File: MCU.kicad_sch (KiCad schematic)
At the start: 42 parts, among them J301 USB_C_Receptacle_USB2.0, J302 Conn_ARM_SWD_TagConnect_TC2030, J303 Screw_Terminal_01x06, SW301 SW_SPDT, U2 STM32H733VGTx, U301 USBLC6-2SC6, Y301 24MHz

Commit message: Refactoring
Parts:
- C301, C318, C319: JLCPCB Part # (none) -> C71001
- C302, C303, C304, C305, C306, C307, C308, C309, C310, C311, C312, C313, C316, C317: JLCPCB Part # (none) -> C432917
- C314, C315: value 14p -> 10p; JLCPCB Part # (none) -> C258501
- D302: JLCPCB Part # (none) -> C3021133; JLCPCB Part# C3021133 -> (none)
- D303: JLCPCB Part # (none) -> C5547384; JLCPCB Part# C5547384 -> (none)
- FB301, FB302: JLCPCB Part # (none) -> C12391
- FL301: JLCPCB Part # (none) -> C3211819; JLCPCB Part# C3211819 -> (none)
- J301: JLCPCB Part # (none) -> C165948; JLCPCB Part# C165948 -> (none)
- J303: JLCPCB Part # (none) -> C3817456; JLCPCB Part# C3817456 -> (none)
- R301: JLCPCB Part # (none) -> C176114
- R302, R305, R306, R307, R308: JLCPCB Part # (none) -> C103557
- R303, R304: JLCPCB Part # (none) -> C325521
- R309, R310: value 325R -> 325R (300R); JLCPCB Part # (none) -> C137637
- R311: JLCPCB Part # (none) -> C328375
- SW301: JLCPCB Part # (none) -> C221841; JLCPCB Part# C221841 -> (none)
- U2: JLCPCB Part # (none) -> C730160; JLCPCB Part# C730160 -> (none)
- U301: JLCPCB Part # (none) -> C5261088; JLCPCB Part# C5261088 -> (none)
- Y301: JLCPCB Part # (none) -> C5308005; JLCPCB Part# C5181479 -> (none)
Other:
- note added: "Cload = 2*(Co-Cs) Co = 10p Cs estimated to be 5p"
- note removed: "Cload = 2*(Co-Cs) Co = 12p Cs estimated to be 5p"

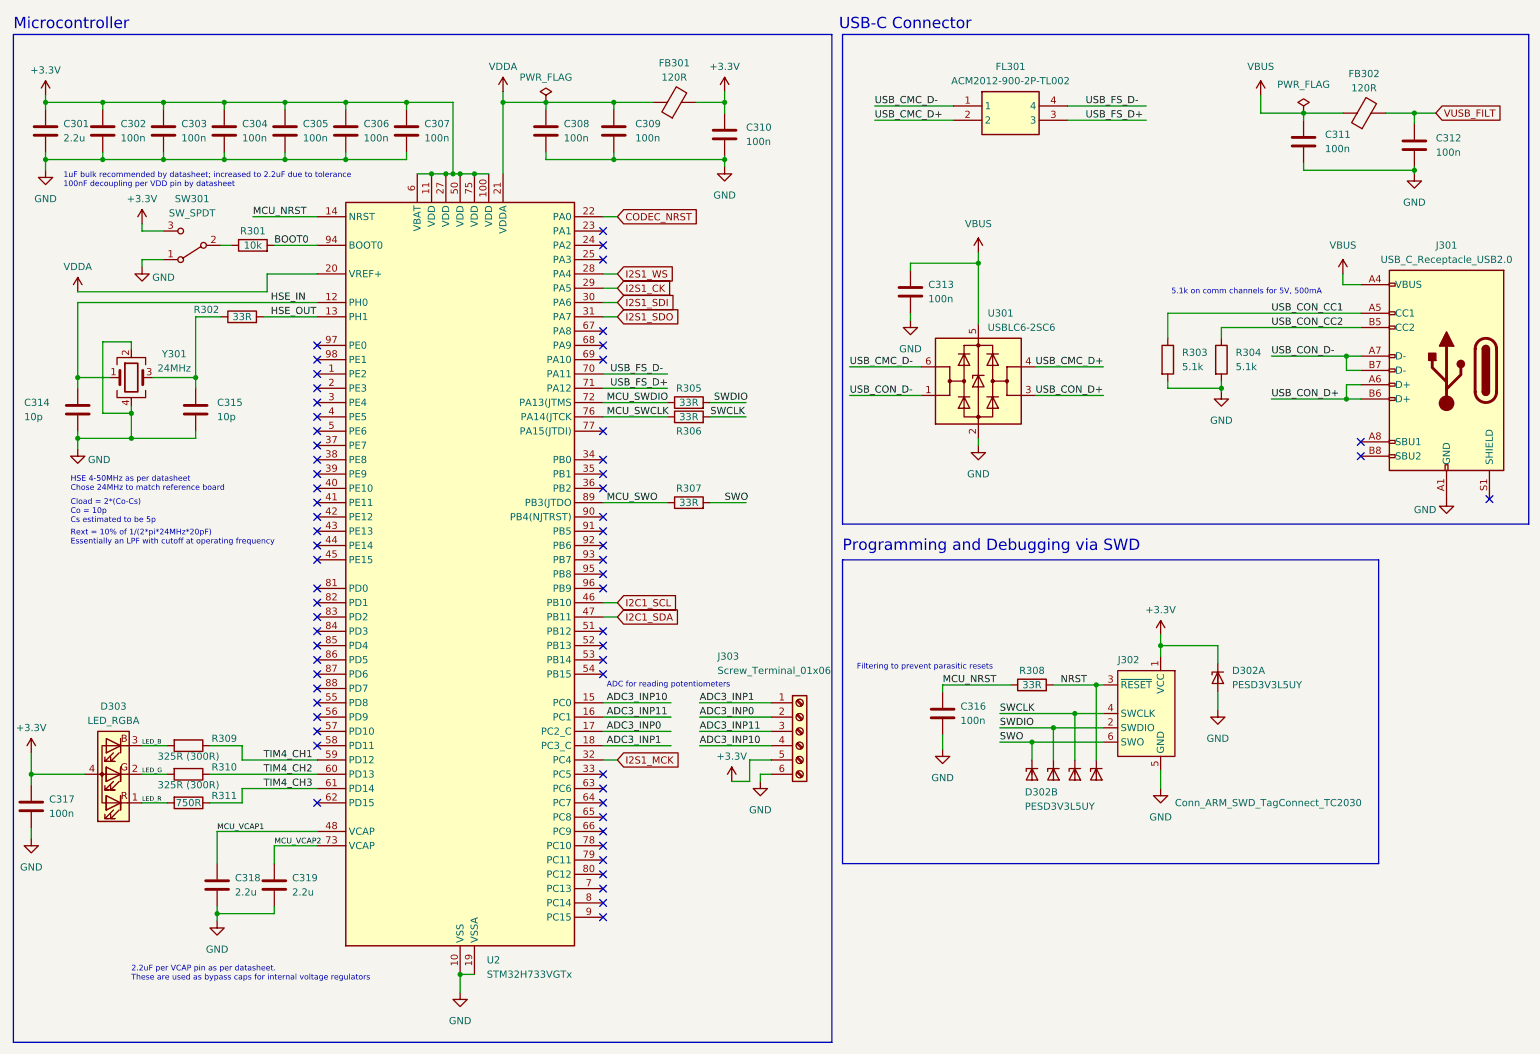
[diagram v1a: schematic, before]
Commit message: Updated 33R resistors to 0R and changed MCU to H723 from H733
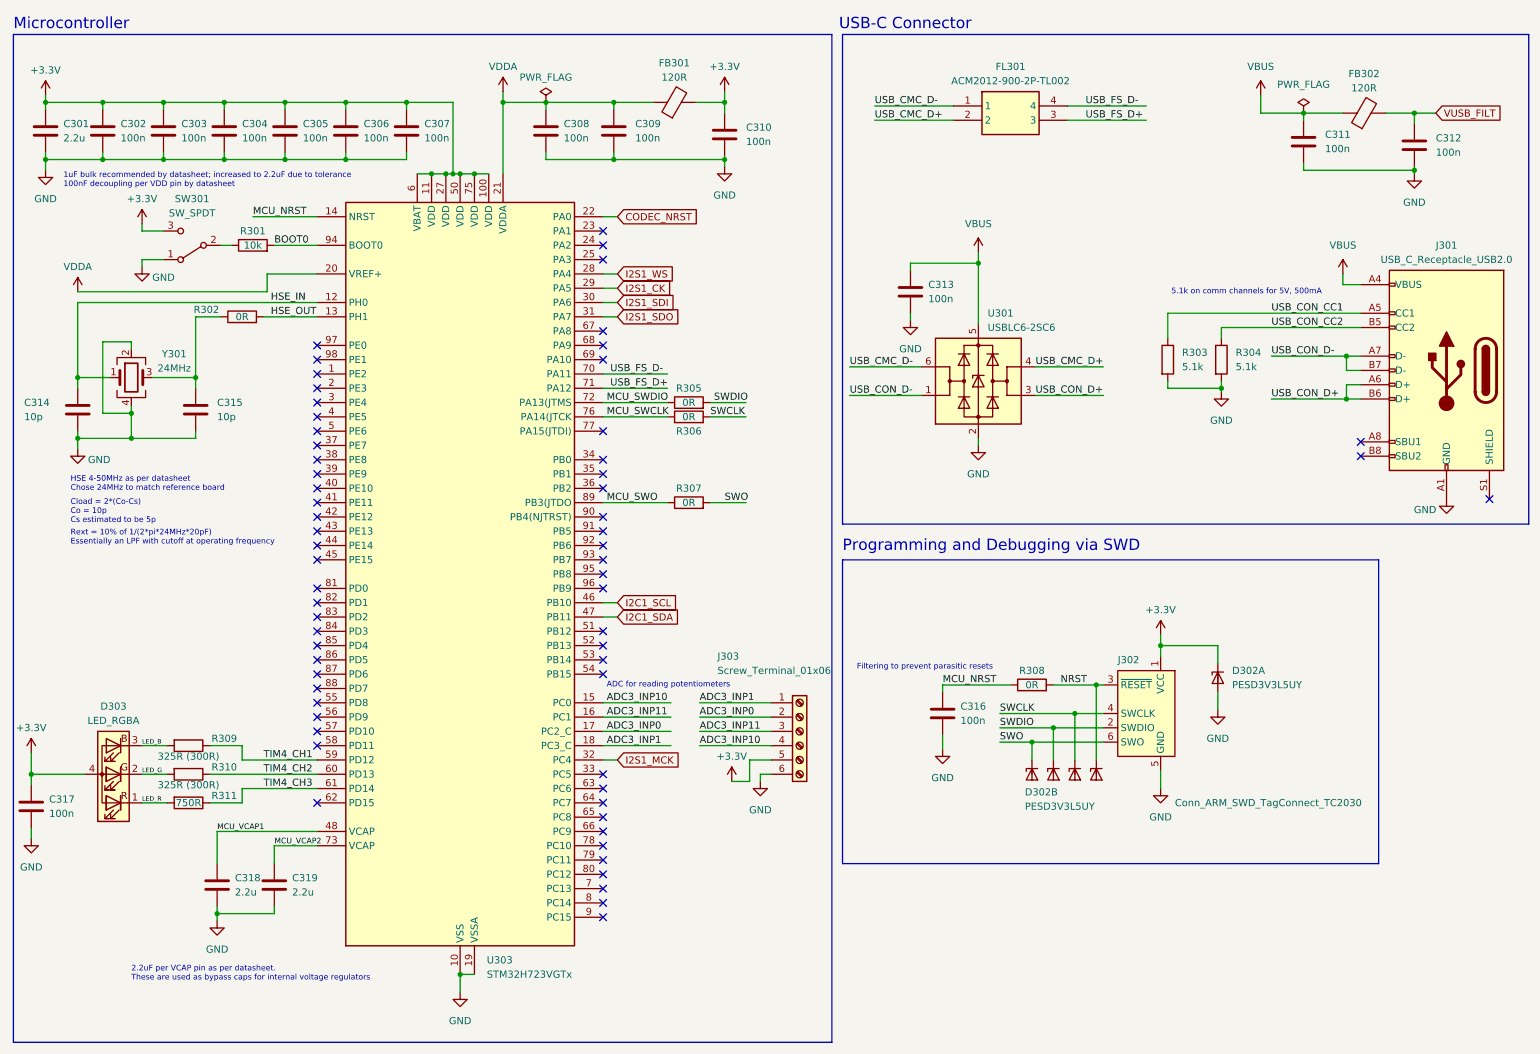
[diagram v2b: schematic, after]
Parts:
- removed U2: STM32H733VGTx, Package_QFP:LQFP-100_14x14mm_P0.5mm, symbol MCU_ST_STM32H7:STM32H733VGTx
- added U303: STM32H723VGTx, Package_QFP:LQFP-100_14x14mm_P0.5mm, symbol MCU_ST_STM32H7:STM32H723VGTx
- R302, R305, R306, R307, R308: value 33R -> 0R; JLCPCB Part # C103557 -> (none)
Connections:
- net +3.3V: now also U303.100 (VDD), U303.11 (VDD), U303.27 (VDD), U303.50 (VDD), U303.6 (VBAT), U303.75 (VDD)
- net ADC3_INP0: now also U303.17 (PC2_C)
- net ADC3_INP1: now also U303.18 (PC3_C)
- net ADC3_INP10: now also U303.15 (PC0)
- net ADC3_INP11: now also U303.16 (PC1)
- net BOOT0: now also U303.94 (BOOT0)
- net CODEC_NRST: now also U303.22 (PA0)
- net GND: now also U303.10 (VSS), U303.19 (VSSA), U303.26 (VSS), U303.49 (VSS), U303.74 (VSS), U303.99 (VSS)
- net HSE_IN: now also U303.12 (PH0)
- net HSE_OUT: now also U303.13 (PH1)
- net I2C1_SCL: now also U303.46 (PB10)
- net I2C1_SDA: now also U303.47 (PB11)
- net I2S1_CK: now also U303.29 (PA5)
- net I2S1_MCK: now also U303.32 (PC4)
- net I2S1_SDI: now also U303.30 (PA6)
- net I2S1_SDO: now also U303.31 (PA7)
- net I2S1_WS: now also U303.28 (PA4)
- net MCU_NRST: now also U303.14 (NRST)
- net MCU_SWCLK: now also U303.76 (PA14(JTCK)
- net MCU_SWDIO: now also U303.72 (PA13(JTMS)
- net MCU_SWO: now also U303.89 (PB3(JTDO)
- net MCU_VCAP1: now also U303.48 (VCAP)
- net MCU_VCAP2: now also U303.73 (VCAP)
- net TIM4_CH1: now also U303.59 (PD12)
- net TIM4_CH2: now also U303.60 (PD13)
- net TIM4_CH3: now also U303.61 (PD14)
- net USB_FS_D+: now also U303.71 (PA12)
- net USB_FS_D-: now also U303.70 (PA11)
- net VDDA: now also U303.20 (VREF+), U303.21 (VDDA)

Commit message: Updated butterworth fc to 25khz, and changed jlc part numbers for resitors and caps
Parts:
- R302, R305, R306, R307, R308: JLCPCB Part # (none) -> C304185

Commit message: Removed CMC and generated new production files
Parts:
- removed FL301: ACM2012-900-2P-TL002, ACM2012-900-2P-TL002:ACM20129002PTL002, symbol ACM2012-900-2P-TL002:ACM2012-900-2P-TL002
- U303: JLCPCB Part # (none) -> C730142
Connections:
- net USB_CMC_D+ is gone; now on net USB_FS_D+: U301.4 (I/O2)
- net USB_CMC_D- is gone; now on net USB_FS_D-: U301.6 (I/O1)
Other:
- note added: "Rext = 10% of 1/(2*pi*24MHz*10pF) Essentially an LPF with cutoff at operating frequency"
- note removed: "Rext = 10% of 1/(2*pi*24MHz*20pF) Essentially an LPF with cutoff at operating frequency"
- moved on the sheet: C311, C312, FB302
